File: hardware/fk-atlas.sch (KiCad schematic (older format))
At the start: 68 parts, among them J1 CONN_02x05_SWD, J10 CONN_01x04, J2 MICRO-USB, J3 CONN_01x02, J4 CONN_01x03_SERIAL, J5 CONN_01x05, J6 CONN_01x04, J7 CONN_01x05, J8 CONN_01x02, J9 MICRO-USB, M1 MOUNT_HOLE, M2 MOUNT_HOLE, M3 MOUNT_HOLE, M4 MOUNT_HOLE, M5 FIDUCIAL, M6 FIDUCIAL, M7 FIDUCIAL, Q4 2N7002LT1G, SW1 SPNO, U1 S25FL116K0XMFI041, U2 ATSAMD21G18A-AU, U3 MCP1700T-3302E/MB, U4 TPS2052B, U5 SK6812, Y1 FC-135

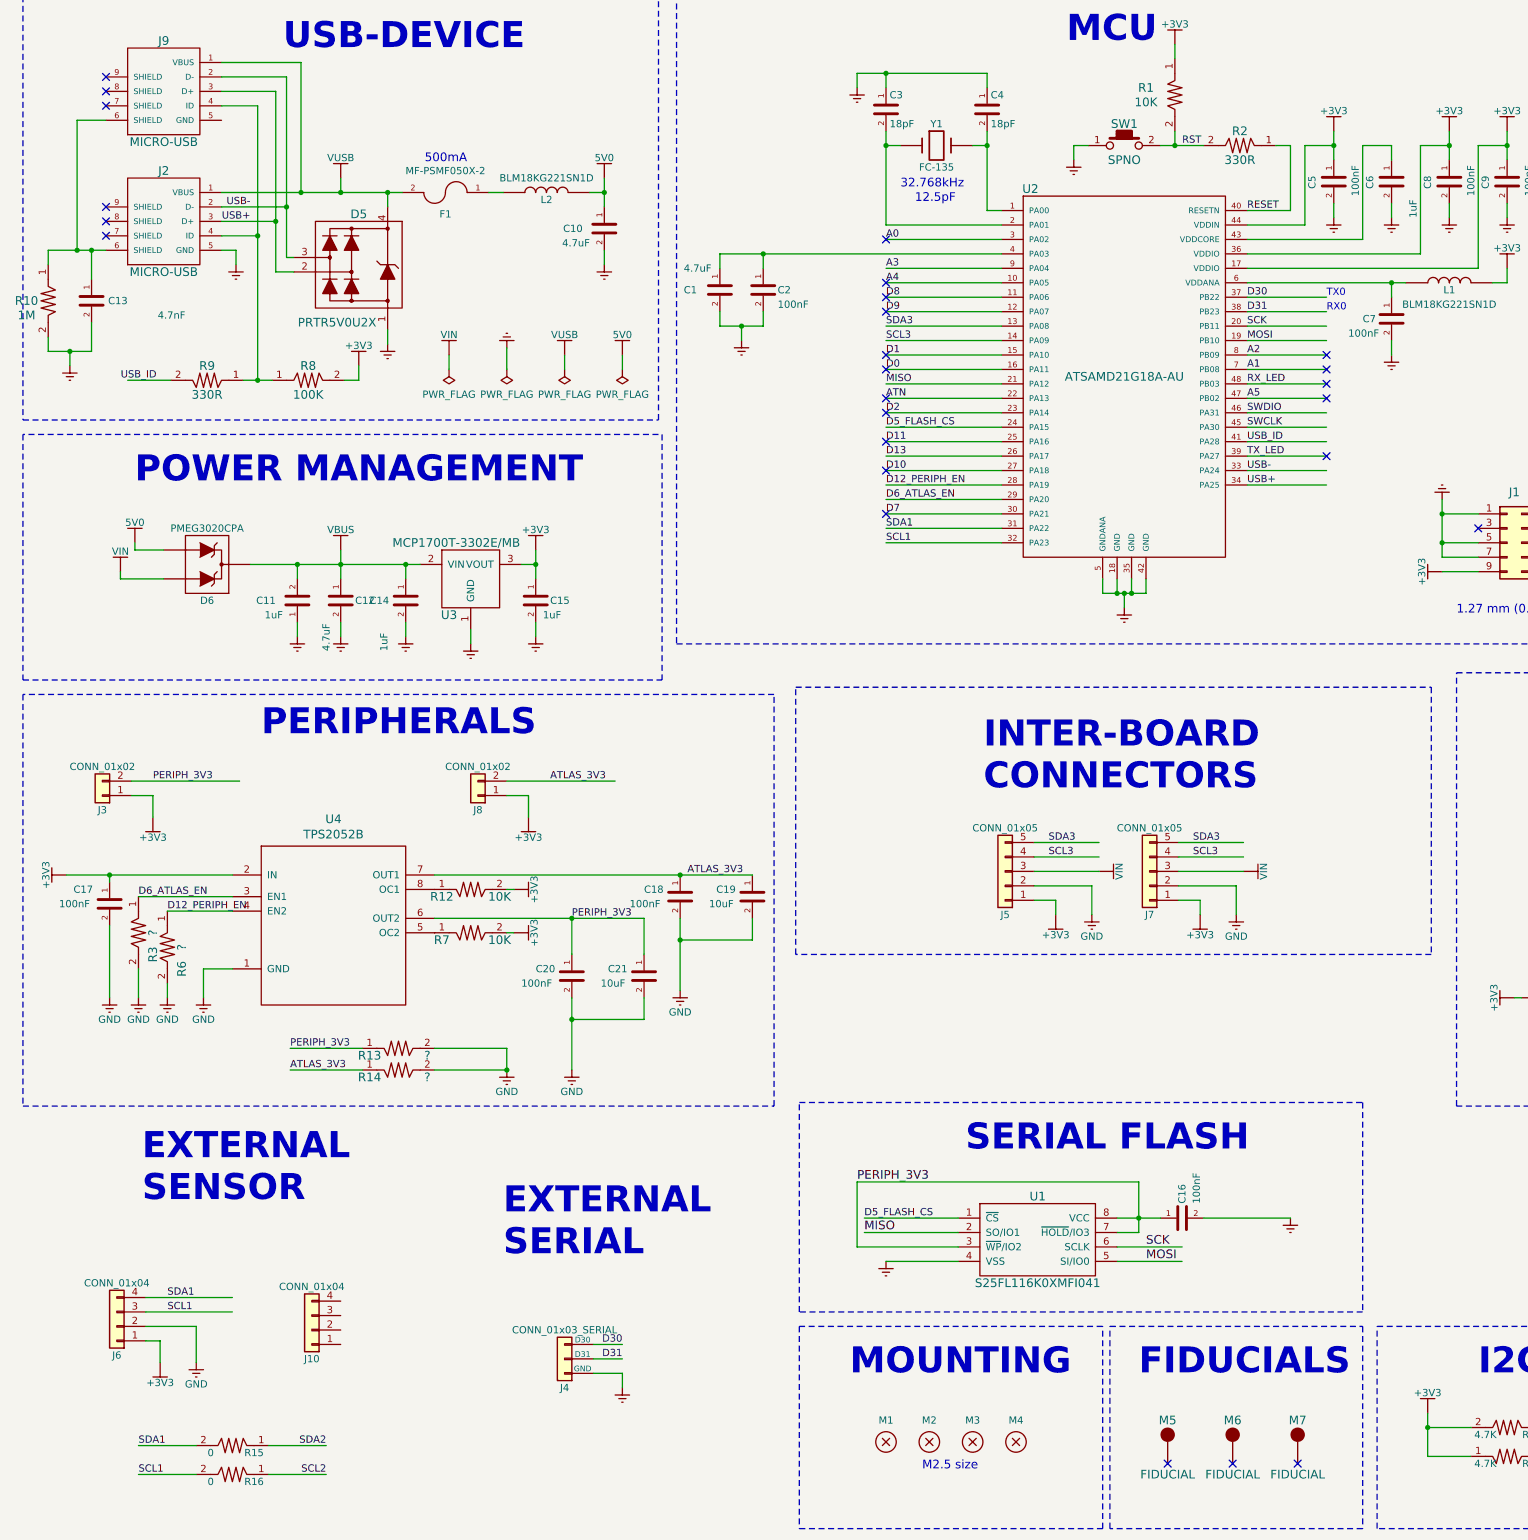
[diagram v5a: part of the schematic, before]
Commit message: Removed VIN connection
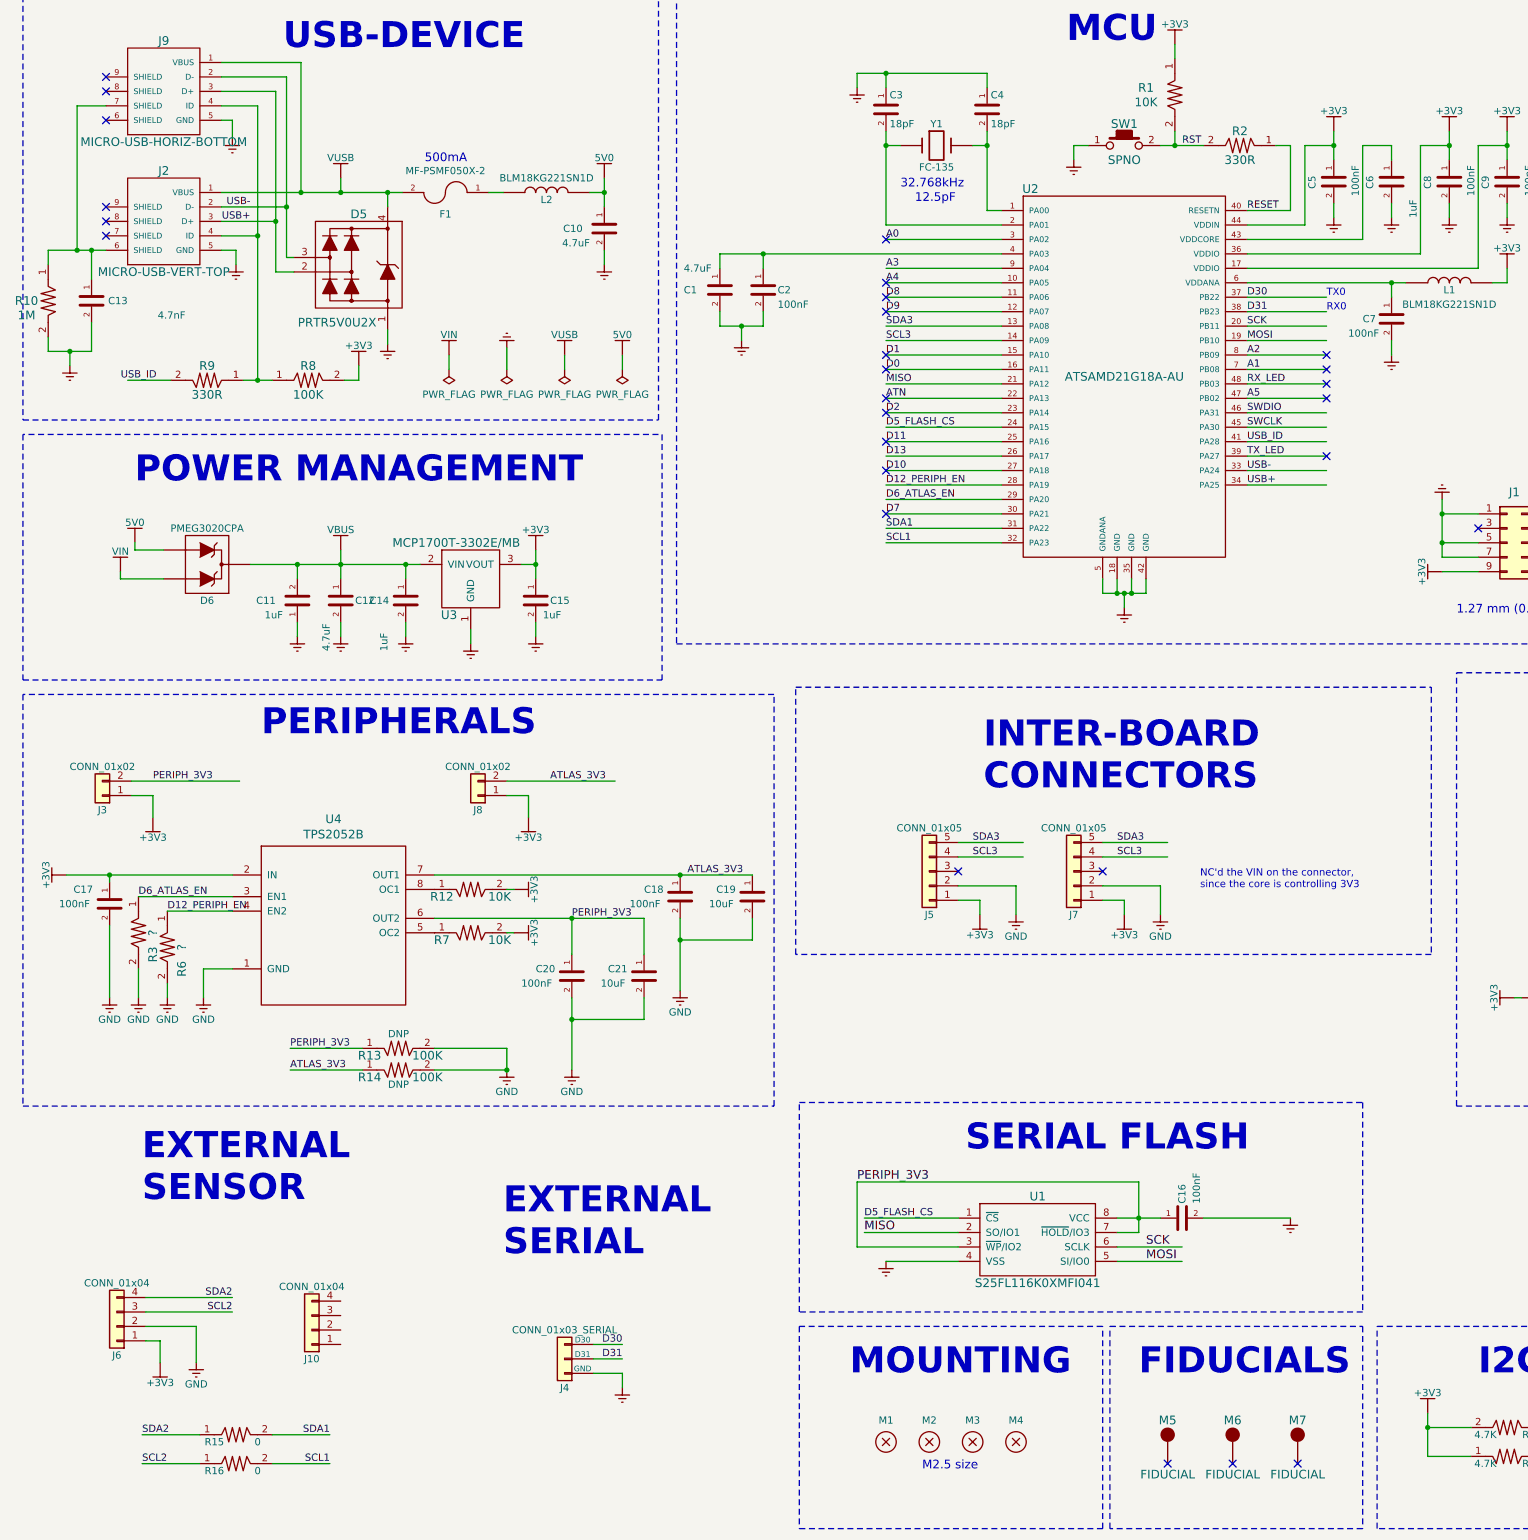
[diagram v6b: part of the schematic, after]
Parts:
- J10: Link (none) -> https://www.digikey.com/product-detail/en/jst-sales-america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; MFN Molex -> (none); MFP 502382-0470 -> (none); SPN1 WM4781CT-ND -> (none)
- J2: value MICRO-USB -> MICRO-USB-VERT-TOP
- J9: value MICRO-USB -> MICRO-USB-HORIZ-BOTTOM
- R13, R14: value ? -> 100K; Population (none) -> DNP
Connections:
- no-connect marks 28 -> 30
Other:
- note added: "NC'd the VIN on the connector, \nsince the core is controlling 3V3"
- moved on the sheet: J5, J7, R15, R16

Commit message: Finished DRC check, no errors
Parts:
- added C22, C23: 10uF, conservify:CAP-0603, symbol fk-atlas-rescue:CAPACITOR_CERAMIC-conservify
- added C24: 100nF, conservify:CAP-0603, symbol fk-atlas-rescue:CAPACITOR_CERAMIC-conservify
- J10: footprint conservify:Molex_CLIK-Mate_502382-0470_1x04_P1.25mm_Vertical -> conservify:BM04B-SRSS-TB; Population (none) -> DNP
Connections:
- wire segments 303 -> 322
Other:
- moved on the sheet: J4, J5, J7

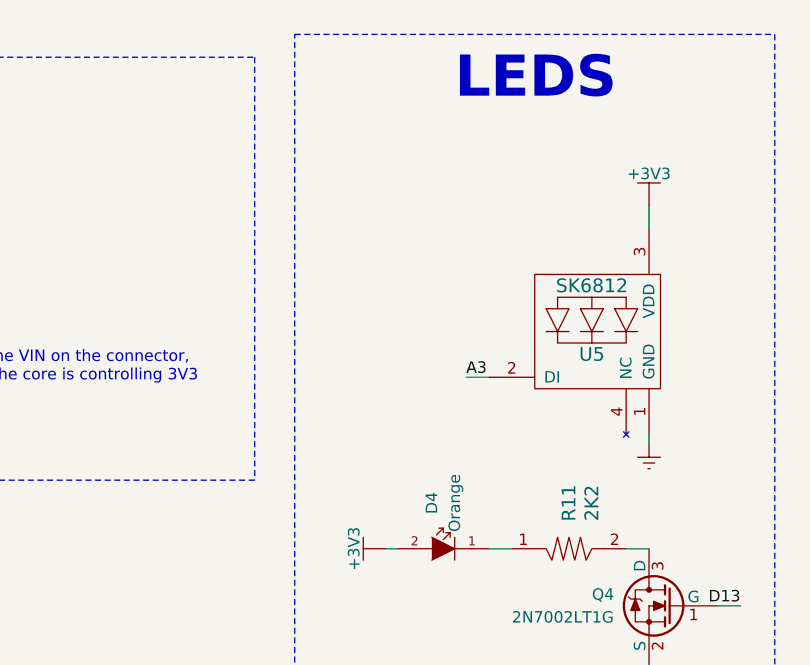
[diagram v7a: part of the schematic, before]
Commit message: Added a power indicator LED, finished touching up traces and added logos, markings back in
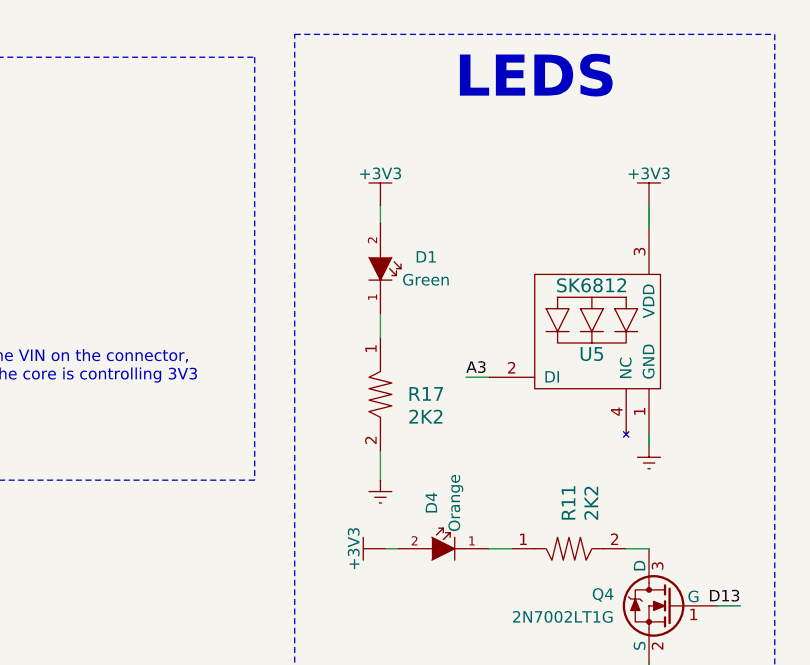
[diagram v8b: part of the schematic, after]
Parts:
- added D1: Green, conservify:LED-0603, symbol fk-atlas-rescue:LED_SINGLE-conservify
- added R17: 2K2, conservify:RES-0603, symbol fk-atlas-rescue:RESISTOR-conservify
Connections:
- wire segments 322 -> 325
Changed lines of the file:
@@
 Wire Notes Line
 	5525 8325 3700 8325
+$Comp
+L fk-atlas-rescue:3V3-conservify #PWR068
+U 1 1 5C6422AC
+P 10825 6000
+F 0 "#PWR068" H 10825 5850 50  0001 C CNN
+F 1 "+3V3" H 10825 6140 50  0000 C CNN
+F 2 "" H 10825 6000 50  0000 C CNN
+F 3 "" H 10825 6000 50  0000 C CNN
+	1    10825 6000
+	1    0    0    -1
+$EndComp
+$Comp
+L fk-atlas-rescue:LED_SINGLE-conservify D1
+U 1 1 5C64234F
+P 10825 6275
+F 0 "D1" V 10875 6075 50  0000 C CNN
+F 1 "Green" V 10775 6075 50  0000 C CNN
+F 2 "conservify:LED-0603" H 10825 6025 60  0001 C CNN
+F 3 "" H 10825 6275 60  0000 C CNN
+F 4 " " H 10875 6175 50  0001 C CNN "Critical"
+F 5 "Lite-On" H 10875 6175 50  0001 C CNN "MFN"
+F 6 "LTST-C190GKT" H 10875 6175 50  0001 C CNN "MFP"
+F 7 " " H 10875 6175 50  0001 C CNN "Notes"
+F 8 " " H 10875 6175 50  0001 C CNN "Package"
+F 9 "ANY" H 10875 6175 50  0001 C CNN "Source"
+F 10 " " H 10875 6175 50  0001 C CNN "Subsystem"
+F 11 "0" H 10875 6175 50  0001 C CNN "price"
+F 12 "859-LTST-C190KFKT" H 9125 75  50  0001 C CNN "spn1"
+F 13 "mouser" H 9125 75  50  0001 C CNN "supplier1"
+	1    10825 6275
+	0    -1   -1   0
+$EndComp
+Wire Wire Line
+	10825 6075 10825 6000
+$Comp
+L fk-atlas-rescue:RESISTOR-conservify R17
+U 1 1 5C663BE7
+P 10825 6825
+F 0 "R17" V 10825 7025 60  0000 C CNN
+F 1 "2K2" V 10925 7025 60  0000 C CNN
+F 2 "conservify:RES-0603" H 10825 6625 60  0001 C CNN
+F 3 "" H 10825 6825 60  0000 C CNN
+F 4 " " H 10825 7125 50  0001 C CNN "Critical"
+F 5 "Yageo" H 10825 7125 50  0001 C CNN "MFN"
+F 6 "RC0603FR-072K2L" H 10825 7125 50  0001 C CNN "MFP"
+F 7 " " H 10825 7125 50  0001 C CNN "Notes"
+F 8 " " H 10825 7125 50  0001 C CNN "Package"
+F 9 "ANY" H 10825 7125 50  0001 C CNN "Source"
+F 10 " " H 10825 7125 50  0001 C CNN "Subsystem"
+F 11 "0" H 10825 7125 50  0001 C CNN "price"
+F 12 "603-RC0603FR-072K2L" H 9125 75  50  0001 C CNN "spn1"
+F 13 "mouser" H 9125 75  50  0001 C CNN "supplier1"
+	1    10825 6825
+	0    1    1    0
+$EndComp
+Wire Wire Line
+	10825 6575 10825 6475
+Wire Wire Line
+	10825 7075 10825 7200
+$Comp
+L fk-atlas-rescue:GND-conservify #PWR069
+U 1 1 5C6A64CF
+P 10825 7200
+F 0 "#PWR069" H 10825 6950 50  0001 C CNN
+F 1 "GND" H 10825 7050 50  0001 C CNN
+F 2 "" H 10825 7200 60  0000 C CNN
+F 3 "" H 10825 7200 60  0000 C CNN
+	1    10825 7200
+	1    0    0    -1
+$EndComp
 $EndSCHEMATC
